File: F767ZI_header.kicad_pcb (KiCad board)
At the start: 2 copper layers, 73 x 98.4 mm, 22 parts, among them J2 CAN1, J3 CAN2, J4 UART, J5 PowerBoard, J6 EMERSW_CON, J7 I2C1_default, J9 RESET_SW, SW1 SW_Push, U1 MCP2562-E-P, U2 MCP2562-E-P

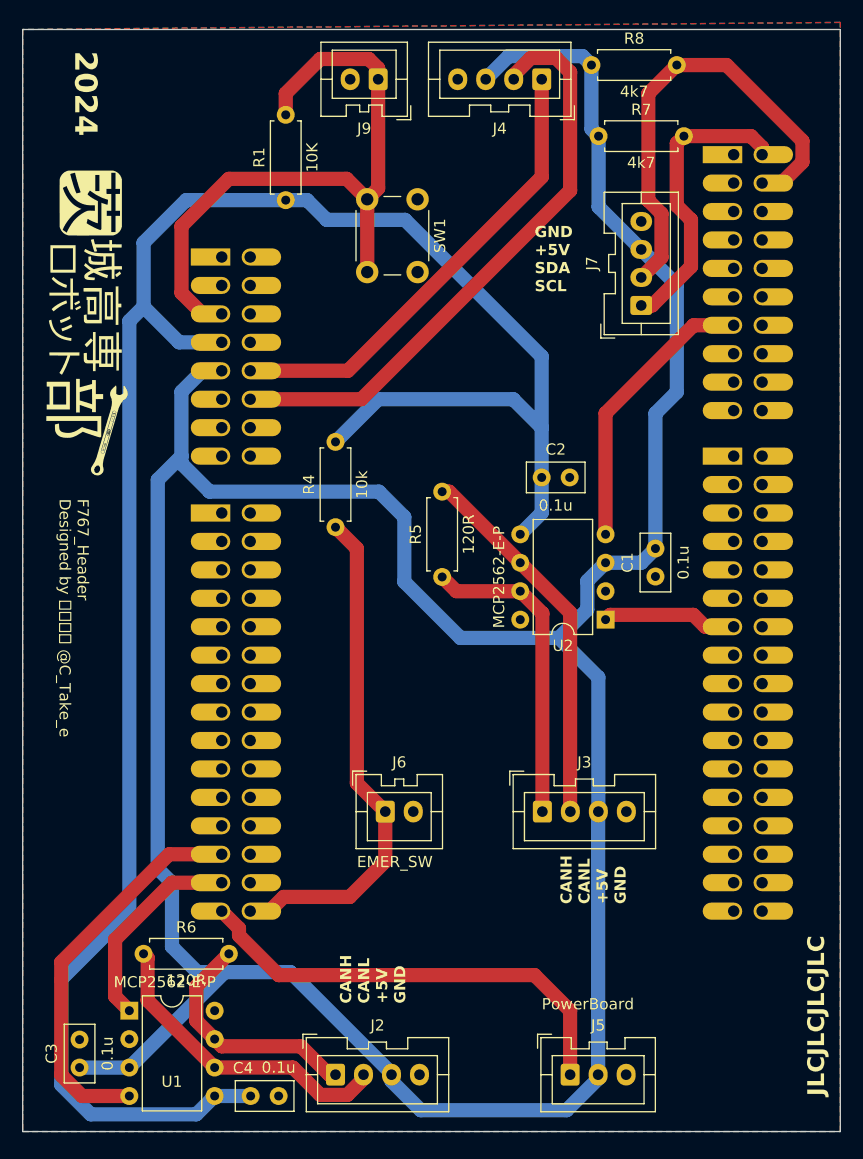
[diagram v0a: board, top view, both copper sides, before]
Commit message: PCB: 外形縮小マン
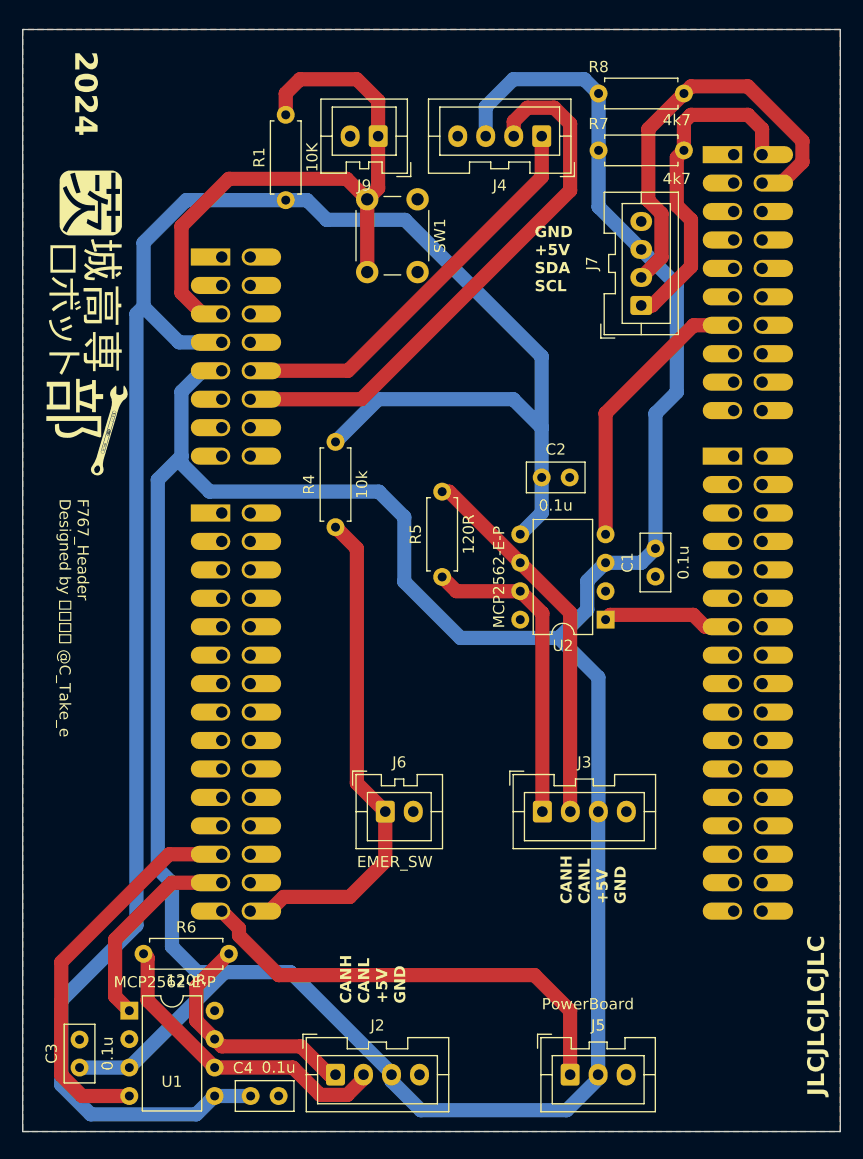
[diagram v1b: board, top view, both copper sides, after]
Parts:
- moved J4 5.08 mm to (200.7, 59.7)
- moved J9 5.08 mm to (186.1, 59.7)
- moved R8 2.62 mm to (205.7, 55.9)
- moved R7 1.27 mm to (205.7, 61.0)
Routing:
- net UART_TX: track 41.9 -> 36.9 mm
- net UART_RX: track 53.4 -> 49.7 mm
- net I2C1_SDA: track 41.6 -> 38.1 mm
- net I2C1_SCL: track 26.4 -> 29.7 mm
- net NRST: track 59.8 -> 56.6 mm
- net +5V: track 275.5 -> 276.3 mm

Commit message: PCB: 永久配置調整タイム
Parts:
- moved SW1 7.43 mm to (184.9, 71.1)
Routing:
- net UART_TX: track 36.9 -> 40.2 mm
- net UART_RX: track 49.7 -> 53.0 mm
- net +5V: track 276.3 -> 275.3 mm
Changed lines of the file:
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@@
 	(footprint "Button_Switch_THT:SW_PUSH_6mm"
 		(layer "F.Cu")
-		(at 189.575 65.33 -90)
+		(at 184.912 71.12 -90)
 		(descr "Generic 6mm SW tactile push button")
 		(tags "tact sw push 6mm")
@@
 		)
 		(property "Value" "MCP2562-E-P"
-			(at 3.165 -2.55 360)
+			(at 2.54 10.16 360)
 			(layer "F.SilkS")
 			(effects
@@
 	)
 	(segment
-		(start 202.89135 146.685)
-		(end 205.7 143.87635)
-		(width 1.27)
-		(layer "B.Cu")
-		(net 3)
-	)
-	(segment
 		(start 209.54205 69.81)
 		(end 209.55 69.81)
@@
 	)
 	(segment
-		(start 205.74 60.96)
-		(end 205.74 66.00795)
+		(start 204.16135 145.415)
+		(end 205.7 143.87635)
 		(width 1.27)
 		(layer "B.Cu")
@@
 	)
 	(segment
-		(start 204.47 54.61)
-		(end 205.74 55.88)
+		(start 205.74 60.96)
+		(end 205.74 66.00795)
 		(width 1.27)
 		(layer "B.Cu")
@@
 	)
 	(segment
-		(start 187.245 144.07295)
-		(end 189.85705 146.685)
+		(start 204.47 54.61)
+		(end 205.74 55.88)
 		(width 1.27)
 		(layer "B.Cu")
@@
 	)
 	(segment
+		(start 187.245 143.51)
+		(end 187.245 144.07295)
+		(width 1.27)
+		(layer "B.Cu")
+		(net 3)
+	)
+	(segment
 		(start 209.55795 69.81)
 		(end 212.725 72.97705)
@@
 	)
 	(segment
-		(start 189.85705 146.685)
-		(end 202.89135 146.685)
+		(start 193.405 104.505)
+		(end 202.2 104.505)
 		(width 1.27)
 		(layer "B.Cu")
@@
 	)
 	(segment
-		(start 193.405 104.505)
-		(end 202.2 104.505)
+		(start 188.58705 145.415)
+		(end 204.16135 145.415)
 		(width 1.27)
 		(layer "B.Cu")
@@
 	)
 	(segment
-		(start 187.245 143.51)
-		(end 187.245 144.07295)
-		(width 1.27)
-		(layer "B.Cu")
-		(net 3)
-	)
-	(segment
 		(start 195.66 57.07)
 		(end 198.12 54.61)
@@
 	)
 	(segment
+		(start 187.245 144.07295)
+		(end 188.58705 145.415)
+		(width 1.27)
+		(layer "B.Cu")
+		(net 3)
+	)
+	(segment
 		(start 166.37 90.38)
 		(end 166.37 125.115)
@@
 	)
 	(segment
-		(start 200.66 79.375)
-		(end 200.66 85.725)
-		(width 1.27)
-		(layer "B.Cu")
-		(net 5)
-	)
-	(segment
-		(start 181.465 67.165)
-		(end 188.45 67.165)
-		(width 1.27)
-		(layer "B.Cu")
-		(net 5)
-	)
-	(segment
 		(start 200.66 85.725)
 		(end 200.66 90.17)
@@
 	)
 	(segment
-		(start 179.705 65.405)
-		(end 181.465 67.165)
+		(start 200.66 90.17)
+		(end 200.66 93.335)
 		(width 1.27)
 		(layer "B.Cu")
@@
 	)
 	(segment
-		(start 200.66 90.17)
-		(end 200.66 93.335)
+		(start 179.705 65.405)
+		(end 183.388 69.088)
 		(width 1.27)
 		(layer "B.Cu")
@@
 	)
 	(segment
-		(start 177.8 65.405)
-		(end 179.705 65.405)
+		(start 190.373 69.088)
+		(end 200.66 79.375)
 		(width 1.27)
 		(layer "B.Cu")
@@
 	)
 	(segment
+		(start 200.66 79.375)
+		(end 200.66 85.725)
+		(width 1.27)
+		(layer "B.Cu")
+		(net 5)
+	)
+	(segment
 		(start 182.245 86.995)
 		(end 186.055 83.185)
@@
 	)
 	(segment
+		(start 183.388 69.088)
+		(end 190.373 69.088)
+		(width 1.27)
+		(layer "B.Cu")
+		(net 5)
+	)
+	(segment
 		(start 177.8 65.405)
-		(end 168.91 65.405)
+		(end 179.705 65.405)
 		(width 1.27)
 		(layer "B.Cu")
@@
 	)
 	(segment
-		(start 188.45 67.165)
-		(end 200.66 79.375)
+		(start 177.8 65.405)
+		(end 168.91 65.405)
 		(width 1.27)
 		(layer "B.Cu")
@@
 	)
 	(segment
-		(start 203.2 58.574325)
-		(end 201.775675 57.15)
+		(start 203.2 70.104)
+		(end 203.2 58.574325)
 		(width 1.27)
 		(layer "F.Cu")
@@
 	)
 	(segment
-		(start 198.16 58.38)
-		(end 198.16 59.69)
+		(start 203.2 58.574325)
+		(end 201.775675 57.15)
 		(width 1.27)
 		(layer "F.Cu")
@@
 	)
 	(segment
-		(start 203.2 64.54224)
-		(end 203.2 58.574325)
+		(start 199.39 57.15)
+		(end 198.16 58.38)
 		(width 1.27)
 		(layer "F.Cu")
@@
 	)
 	(segment
-		(start 184.55724 83.185)
-		(end 203.2 64.54224)
+		(start 198.16 58.38)
+		(end 198.16 59.69)
 		(width 1.27)
 		(layer "F.Cu")
@@
 	)
 	(segment
-		(start 201.775675 57.15)
-		(end 199.39 57.15)
+		(start 174.625 83.185)
+		(end 190.119 83.185)
 		(width 1.27)
 		(layer "F.Cu")
@@
 	)
 	(segment
-		(start 174.625 83.185)
-		(end 184.55724 83.185)
+		(start 190.119 83.185)
+		(end 203.2 70.104)
 		(width 1.27)
 		(layer "F.Cu")
@@
 	)
 	(segment
-		(start 199.39 57.15)
-		(end 198.16 58.38)
+		(start 201.775675 57.15)
+		(end 199.39 57.15)
 		(width 1.27)
 		(layer "F.Cu")
@@
 	)
 	(segment
-		(start 183.355082 80.645)
-		(end 200.66 63.340082)
+		(start 174.625 80.645)
+		(end 189.103 80.645)
 		(width 1.27)
 		(layer "F.Cu")
@@
 	)
 	(segment
-		(start 174.625 80.645)
-		(end 183.355082 80.645)
+		(start 189.103 80.645)
+		(end 200.66 69.088)
 		(width 1.27)
 		(layer "F.Cu")
@@
 	)
 	(segment
-		(start 200.66 63.340082)
+		(start 200.66 69.088)
 		(end 200.66 59.69)
 		(width 1.27)
@@
 	)
 	(segment
-		(start 186.055 59.69)
-		(end 186.055 64.35)
+		(start 168.485 73.687742)
+		(end 168.485 68.885)
 		(width 1.27)
 		(layer "F.Cu")
@@
 	)
 	(segment
-		(start 172.085 75.565)
-		(end 170.362258 75.565)
+		(start 179.702 67.362)
+		(end 180.412 68.072)
 		(width 1.27)
 		(layer "F.Cu")
@@
 	)
 	(segment
-		(start 186.055 64.35)
-		(end 185.075 65.33)
+		(start 170.008 67.362)
+		(end 179.702 67.362)
 		(width 1.27)
 		(layer "F.Cu")
@@
 	)
 	(segment
-		(start 168.485 67.735)
-		(end 172.72 63.5)
+		(start 186.055 61.719)
+		(end 180.412 67.362)
 		(width 1.27)
 		(layer "F.Cu")
@@
 	)
 	(segment
-		(start 185.075 65.33)
-		(end 185.075 71.83)
+		(start 172.085 75.565)
+		(end 170.362258 75.565)
+		(width 1.27)
+		(layer "F.Cu")
+		(net 8)
+	)
+	(segment
+		(start 186.055 59.69)
+		(end 186.055 61.719)
 		(width 1.27)
 		(layer "F.Cu")
@@
 	)
 	(segment
-		(start 172.72 63.5)
-		(end 183.245 63.5)
+		(start 180.412 67.362)
+		(end 180.412 68.072)
 		(width 1.27)
 		(layer "F.Cu")
@@
 	)
 	(segment
-		(start 168.485 73.687742)
-		(end 168.485 67.735)
+		(start 168.485 68.885)
+		(end 170.008 67.362)
 		(width 1.27)
 		(layer "F.Cu")
@@
 	)
 	(segment
-		(start 183.245 63.5)
-		(end 185.075 65.33)
+		(start 170.362258 75.565)
+		(end 168.485 73.687742)
+		(width 1.27)
+		(layer "F.Cu")
+		(net 8)
+	)
+	(segment
+		(start 180.412 68.072)
+		(end 180.412 71.12)
 		(width 1.27)
 		(layer "F.Cu")
@@
 	)
 	(segment
-		(start 177.8 57.785)
-		(end 177.8 55.88)
+		(start 180.412 71.12)
+		(end 180.412 77.62)
 		(width 1.27)
 		(layer "F.Cu")
@@
 	)
 	(segment
-		(start 170.362258 75.565)
-		(end 168.485 73.687742)
+		(start 177.8 57.785)
+		(end 177.8 55.88)
 		(width 1.27)
 		(layer "F.Cu")
